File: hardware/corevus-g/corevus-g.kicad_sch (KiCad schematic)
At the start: 195 parts, among them J1 USB 2.0, J10 JST XH, J11 JST XH, J12 JST XH, J13 EXP1, J14 JST XH, J15 XH, J16 JST XH, J17 JST XH, J18 JST XH, J19 JST XH, J2 JST XH, J28 EXP2, J3 Power In, J32 JST XH, J33 JST XH, J34 JST XH, J35 JST XH, J36 Conn_02x09_Odd_Even, J4 XH, J5 XH, J6 XH, J7 JST XH, J8 JST XH, J9 JST XH, Q22 AO3400, Q26 60N03F, Q27 AO3400, Q28 AO3400, Q29 AO3400, Q30 AO3400, Q31 AO3400, Q32 AO3400, SW1 SW_SPDT, SW2 SW_SPDT, SW3 SPST, SW9 SW_SPDT, U1 STM32F407ZETx, U14 CD4504B, U15 RT8110B, U4 SRV05-4, U5 RT8110B, U6 AMS1117-3.3, Y1 12 MHz

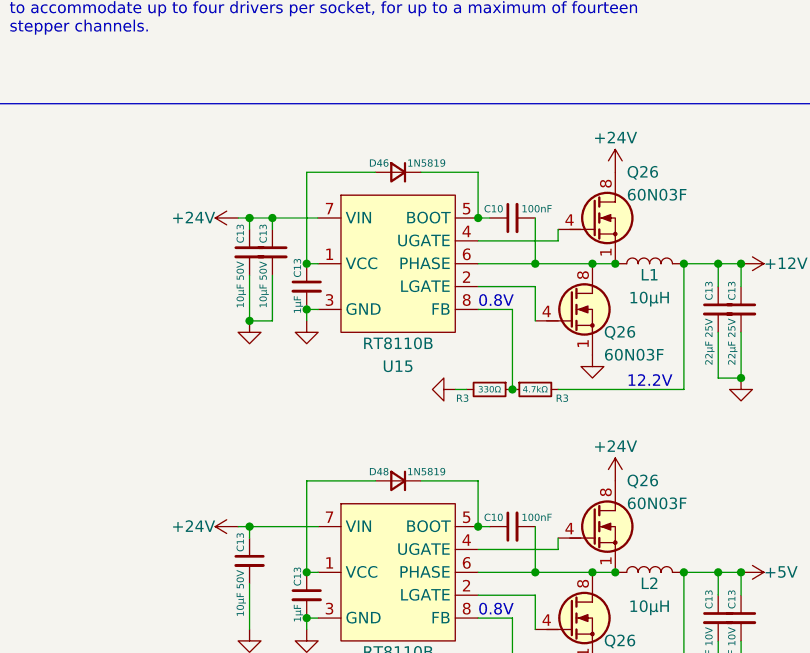
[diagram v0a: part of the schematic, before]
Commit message: finish corevus-g, create file for corevus-k
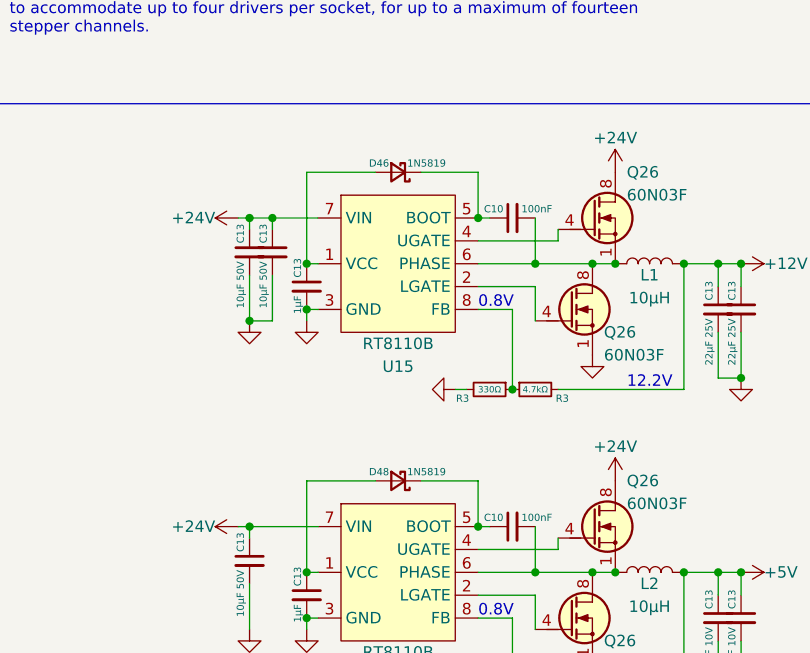
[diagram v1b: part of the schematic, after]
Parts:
- D46, D48: symbol Device:D_Small -> Device:D_Schottky_Small

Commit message: test
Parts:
- removed J36: Conn_02x09_Odd_Even, Connector_PinSocket_2.54mm:PinSocket_2x09_P2.54mm_Vertical, symbol Connector_Generic:Conn_02x09_Odd_Even
- added J25, J29, J30: 1x6, corevus:PinHeader_1x06_P2.54mm_Vertical, symbol Connector:Conn_01x06_Pin
- F1, F2, F3, F4, F5, F6: footprint corevus:XF-505P -> corevus:XF-506P
- R3: value 200Ω -> 470Ω
- R3: value 1kΩ -> 10kΩ
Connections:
- net +12V: now also J29.1 (Pin_1), J29.2 (Pin_2), J29.3 (Pin_3), J29.4 (Pin_4), J29.5 (Pin_5), J29.6 (Pin_6)
- net +24V: now also J33.2 (Pin_2), J34.2 (Pin_2), J35.2 (Pin_2), J30.1 (Pin_1), J30.2 (Pin_2), J30.3 (Pin_3), J30.4 (Pin_4), J30.5 (Pin_5), J30.6 (Pin_6); no longer J33.1 (Pin_1), J34.1 (Pin_1), J35.1 (Pin_1)
- net F0_V+: now also J14.2 (Pin_2), J25.1 (Pin_1); no longer J14.1 (Pin_1)
- net F1_V+: now also J16.2 (Pin_2), J25.2 (Pin_2); no longer J16.1 (Pin_1)
- net F2_V+: now also J17.2 (Pin_2), J25.3 (Pin_3); no longer J17.1 (Pin_1)
- net F3_V+: now also J18.2 (Pin_2), J25.4 (Pin_4); no longer J18.1 (Pin_1)
- net F4_V+: now also J19.2 (Pin_2), J25.5 (Pin_5); no longer J19.1 (Pin_1)
- net F5_V+: now also J32.2 (Pin_2), J25.6 (Pin_6); no longer J32.1 (Pin_1)
- net GND: now also J14.1 (Pin_1), J16.1 (Pin_1); no longer J14.2 (Pin_2), J16.2 (Pin_2)
- net LCD_Rs: now also U1.80 (PD11)
- net ~{Reset}: now also C10.1, R3.2, SW3.2, U1.25 (NRST)
- net at D39.2 (A), Q31.3 (D): now also J34.1 (Pin_1); no longer J34.2 (Pin_2)
- net at D38.2 (A), Q30.3 (D): now also J33.1 (Pin_1); no longer J33.2 (Pin_2)
- net at D31.2 (A), Q27.3 (D): now also J18.1 (Pin_1); no longer J18.2 (Pin_2)
- net at D30.2 (A), Q22.3 (D): now also J17.1 (Pin_1); no longer J17.2 (Pin_2)
- net at D36.2 (A), Q28.3 (D): now also J19.1 (Pin_1); no longer J19.2 (Pin_2)
- net at D37.2 (A), Q29.3 (D): now also J32.1 (Pin_1); no longer J32.2 (Pin_2)
- net at D41.2 (A), Q32.3 (D): now also J35.1 (Pin_1); no longer J35.2 (Pin_2)
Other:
- moved on the sheet: J13, J17, J18, J19, J28, J32, J33, J34, J35
